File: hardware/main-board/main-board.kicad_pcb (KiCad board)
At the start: 4 copper layers, 105 x 38 mm, 78 parts, among them J1 USB_B_Micro, J2 DNI, J3 Display Connector, J4 Conn_01x02, SW1 SW_Push, SW2 SW_Push, SW3 SW_Push, SW4 SW_Push, SW5 SW_Detect, U1 TSL2591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

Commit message: Change MCU component value to 64KB flash variant
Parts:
- U2: value STM32L052K6U6 -> STM32L052K8U6

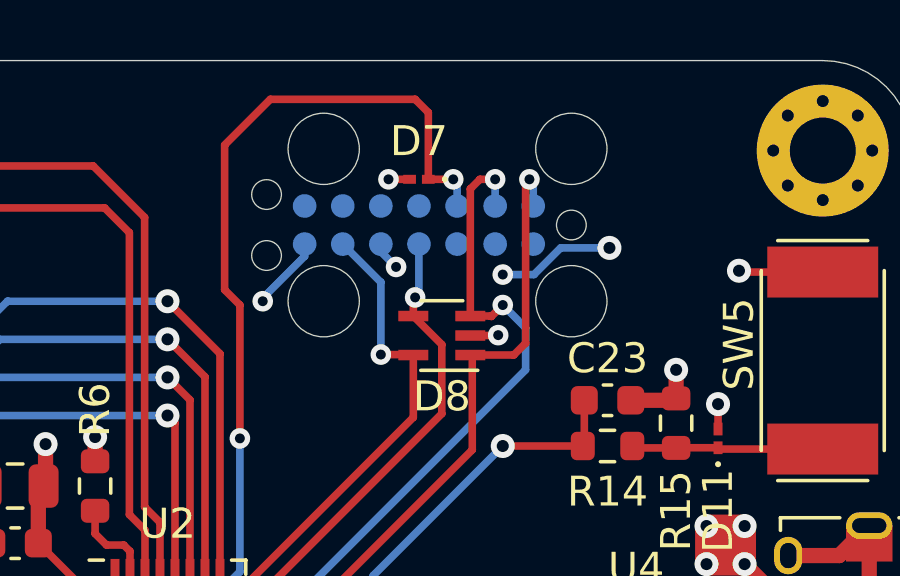
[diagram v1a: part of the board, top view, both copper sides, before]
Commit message: Connect power to debug connector
This allows the ST-Link to detect the target voltage, but otherwise
isn't really necessary. Still probably a good idea to have, though.
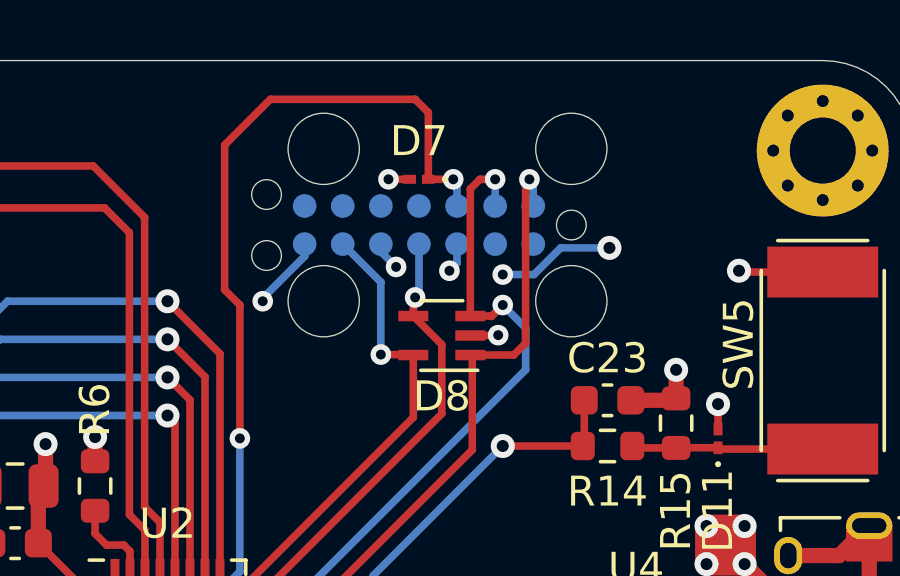
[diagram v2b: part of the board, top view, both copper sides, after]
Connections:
- J2 pad 3: Net-(J2-Pad3) -> +3V3
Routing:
- net +3V3: track 29.1 -> 30.1 mm, vias 10 -> 11

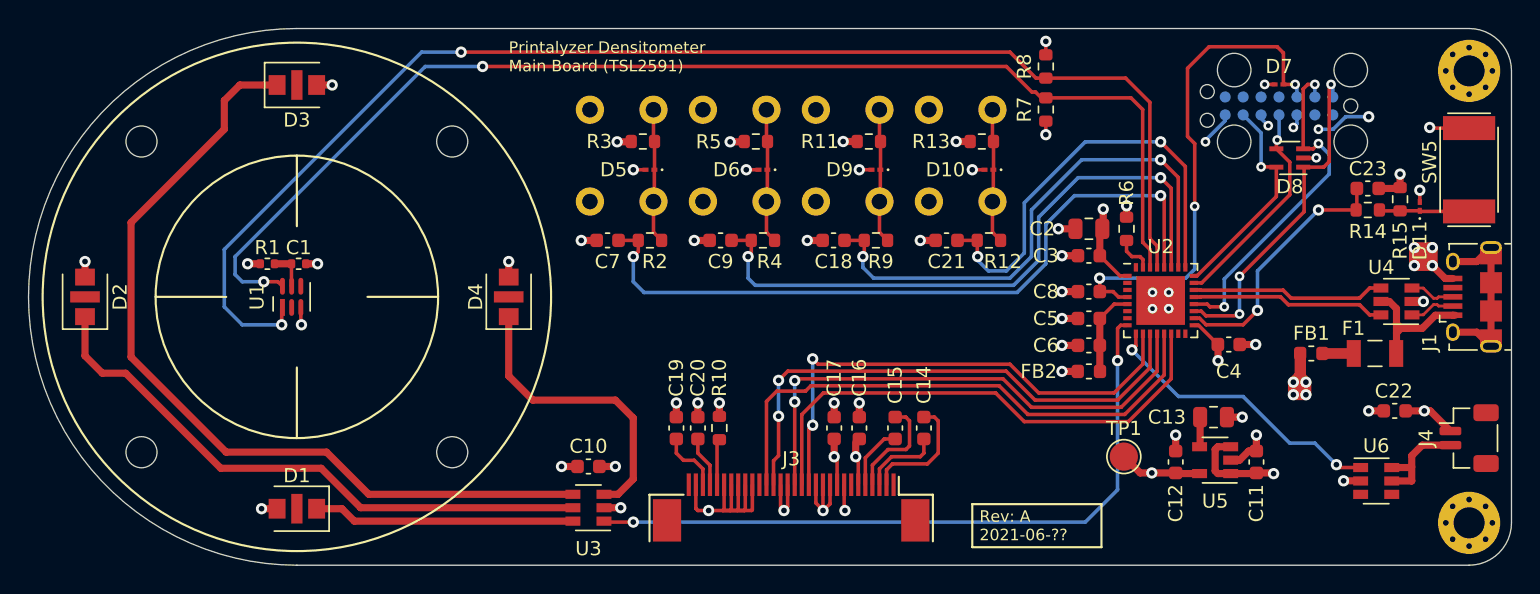
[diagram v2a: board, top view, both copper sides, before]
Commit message: Moved debug connector and minor trace cleanup
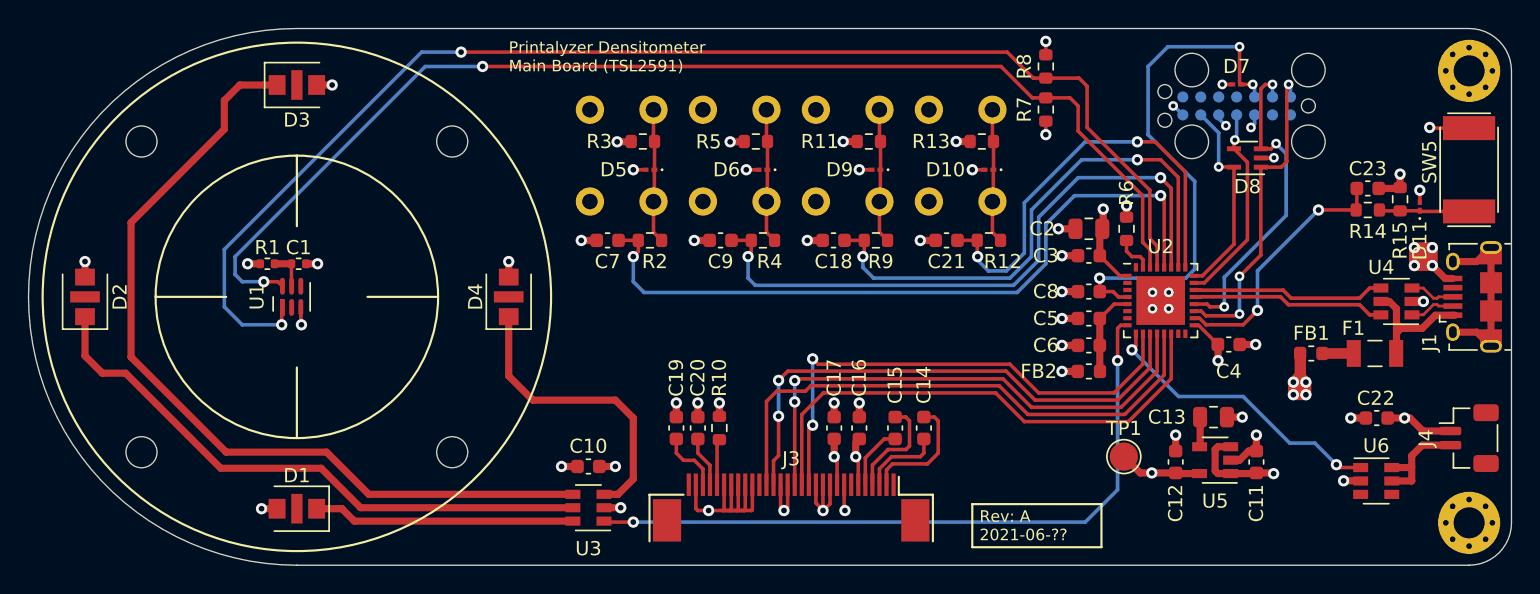
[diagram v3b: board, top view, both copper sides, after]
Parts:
- moved D7 3.00 mm to (126.5, 45.0)
- moved D8 3.00 mm to (127.3, 50.2)
- moved J2 3.00 mm to (126.5, 46.5)
- moved C22 1.37 mm to (136.5, 68.6)
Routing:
- net GND: track 74.5 -> 69.0 mm, vias 54 -> 52
- net /I2C1_SDA: track 87.5 -> 84.9 mm
- net /I2C1_SCL: track 94.6 -> 92.7 mm
- net /USART1_RX: track 24.4 -> 23.2 mm
- net /RESET: track 36.1 -> 37.3 mm
- net /USART1_TX: track 24.1 -> 22.9 mm
- net +5V: track 26.0 -> 27.2 mm
- net /SWDIO: track 15.5 -> 14.4 mm
- net /SWCLK: track 15.5 -> 14.8 mm

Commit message: Updated properties, silkscreen, and page markings for Rev A
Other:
- board text added: "Rev: A 2021-06-15"
- board text removed: "Rev: A 2021-06-??"
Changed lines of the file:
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@@
   (title_block
     (title "Printalyzer Densitometer - Main Board")
-    (date 2021-06-??)
+    (date 2021-06-15)
     (rev A)
     (company LogicProbe.org)
@@
     (pcbplotparams
       (layerselection 0x010fc_ffffffff)
-      (usegerberextensions false)
-      (usegerberattributes true)
-      (usegerberadvancedattributes true)
-      (creategerberjobfile true)
+      (usegerberextensions true)
+      (usegerberattributes false)
+      (usegerberadvancedattributes false)
+      (creategerberjobfile false)
       (excludeedgelayer true)
-      (linewidth 0.100000)
+      (linewidth 0.150000)
       (plotframeref false)
       (viasonmask false)
@@
       (plotvalue false)
       (plotinvisibletext false)
-      (padsonsilk true)
-      (subtractmaskfromsilk false)
+      (padsonsilk false)
+      (subtractmaskfromsilk true)
       (outputformat 1)
       (mirror false)
@@
       (effects (font (size 1 1) (thickness 0.15)))
     )
-    (pad MP smd roundrect (at 1.8 -1.2 270) (size 1.2 1.8) (layers F.Cu F.Paste F.Mask) (roundrect_rratio 0.208333))
-    (pad MP smd roundrect (at -1.8 -1.2 270) (size 1.2 1.8) (layers F.Cu F.Paste F.Mask) (roundrect_rratio 0.208333))
+    (pad MP smd roundrect (at 1.8 -1.2 270) (size 1.2 1.8) (layers F.Cu F.Paste F.Mask) (roundrect_rratio 0.2083325))
+    (pad MP smd roundrect (at -1.8 -1.2 270) (size 1.2 1.8) (layers F.Cu F.Paste F.Mask) (roundrect_rratio 0.2083325))
     (pad 2 smd roundrect (at 0.5 1.325 270) (size 0.6 1.55) (layers F.Cu F.Paste F.Mask) (roundrect_rratio 0.25)
       (net 68 "Net-(J4-Pad2)"))
@@
     (tags resistor)
     (attr smd)
-    (fp_text reference R6 (at 2.54 0 90) (layer F.SilkS)
+    (fp_text reference R6 (at 2.8575 0 90) (layer F.SilkS)
       (effects (font (size 1 1) (thickness 0.15)))
     )
@@
     (arrow2b (pts (xy 146 33.500001) (xy 144.873496 34.086422)))
   )
-  (gr_text "Rev: A\n2021-06-??" (at 114.284 67.585 180) (layer B.SilkS)
+  (gr_text "Rev: A\n2021-06-15" (at 114.284 67.585 180) (layer B.SilkS)
     (effects (font (size 0.8128 0.8128) (thickness 0.1524)) (justify left mirror))
   )
@@
   (gr_line (start 107.823 77.724) (end 116.967 77.724) (layer F.SilkS) (width 0.1524))
   (gr_line (start 107.823 74.676) (end 107.823 77.724) (layer F.SilkS) (width 0.1524))
-  (gr_text "Rev: A\n2021-06-??" (at 108.331 76.2) (layer F.SilkS)
+  (gr_text "Rev: A\n2021-06-15" (at 108.331 76.2) (layer F.SilkS)
     (effects (font (size 0.8128 0.8128) (thickness 0.1524)) (justify left))
   )

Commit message: Removed date and revision markings in prep for updates
This is to prevent old values from being left in the next revision. New
values will be added when Rev B is finished.
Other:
- board text added: "Rev: ? 2021-??-??"
- board text removed: "Rev: A 2021-06-15"

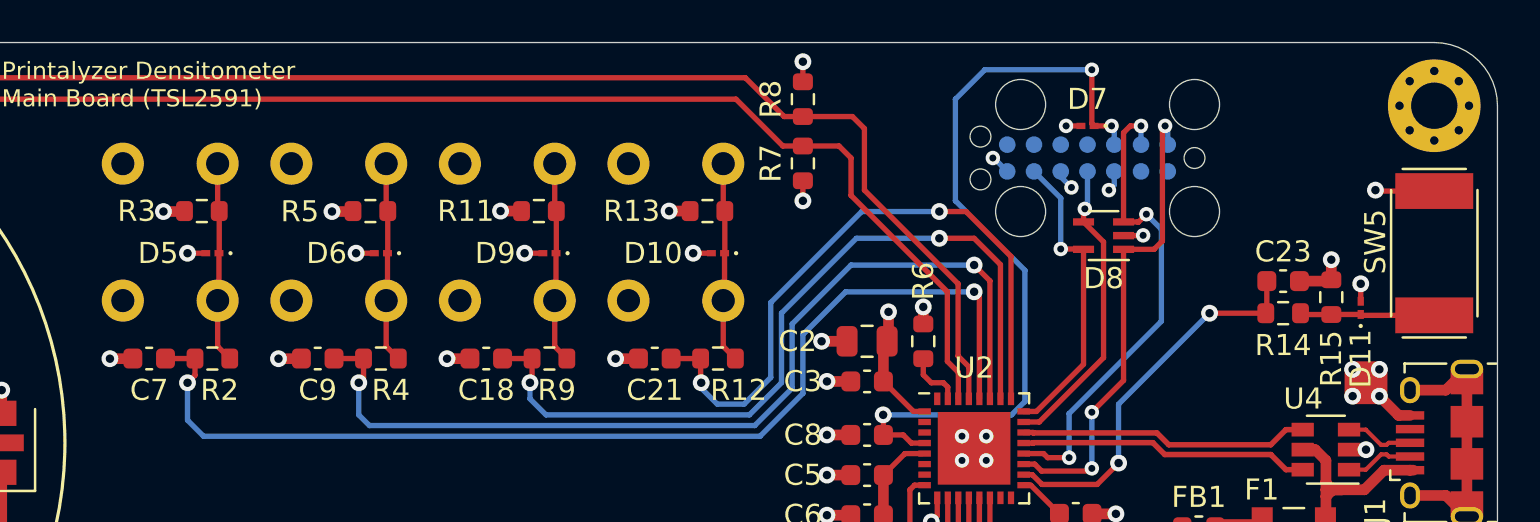
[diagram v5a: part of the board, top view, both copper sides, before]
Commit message: Switch single-line TVS diode components
Switch the existing single-line TVS diodes to a slightly larger
component.

Refs #10
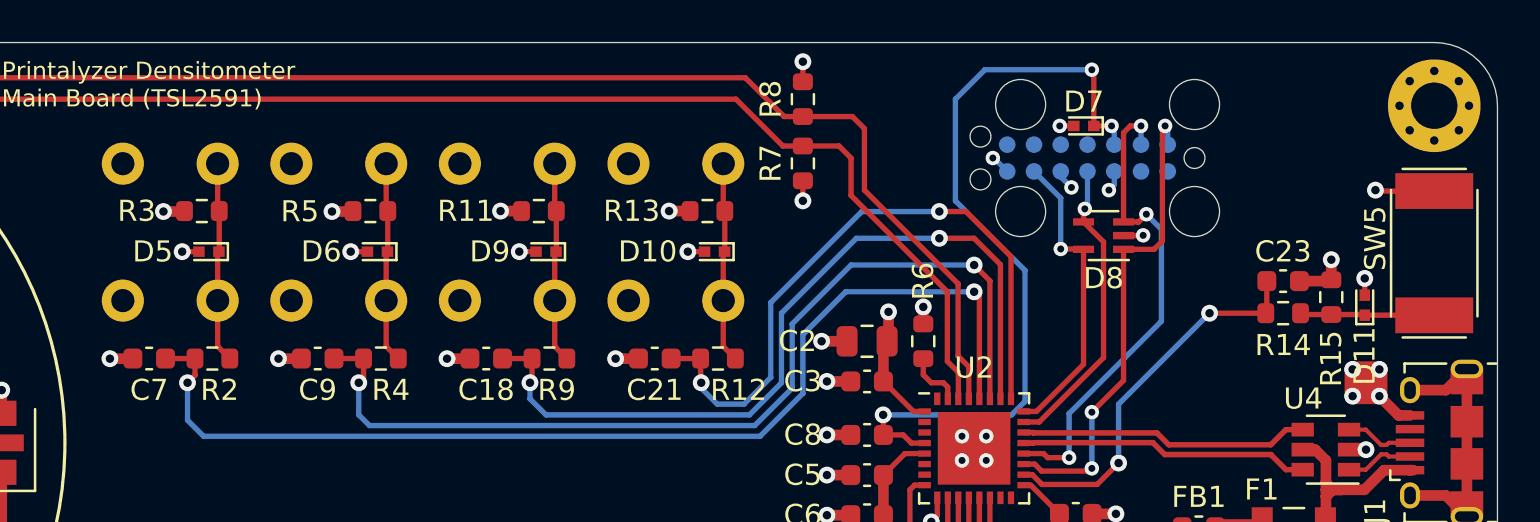
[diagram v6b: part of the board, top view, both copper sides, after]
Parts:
- D10, D11, D5, D6, D7, D9: value ESDALC6V1-1U2 -> ESDALC6V1-1M2; footprint lib_fp:ST0201 -> lib_fp:D_SOD-882
- moved D11 0.23 mm to (139.7, 53.5)
- moved D5 0.18 mm to (84.8, 50.9)
- moved D6 0.18 mm to (92.8, 50.9)
- moved D9 0.18 mm to (100.8, 50.9)
- moved D10 0.18 mm to (108.8, 50.9)
- moved D7 0.18 mm to (126.4, 45.0)

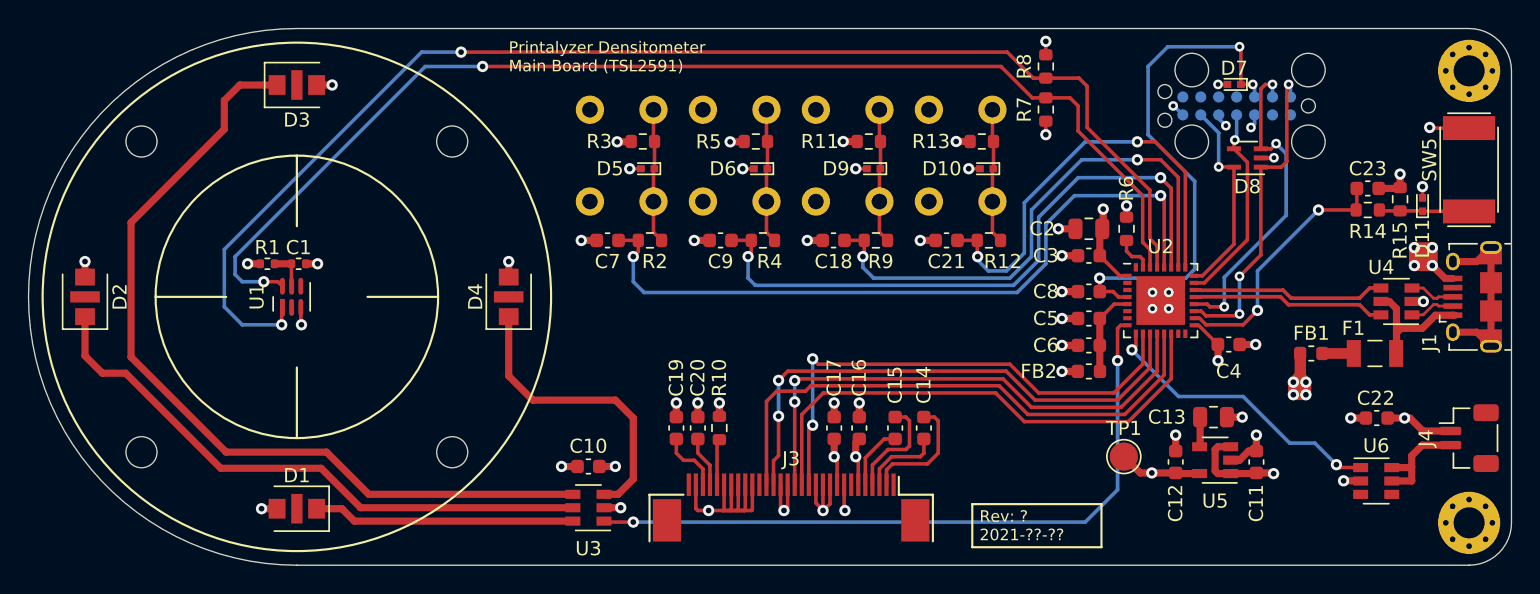
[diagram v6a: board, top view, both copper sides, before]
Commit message: Changed MCU on main board and routed pin changes
Swapped the MCU from the L052K to the K072K, pulling in all pin
assignment changes from the CubeMX data.

Added extra bypass capacitor and sensor interrupt (/w pull-up) to
schematic.

Updated PCB routing to reflect changes, which included rearranging the
layout of many bypass capacitors and making a variety of adjustments to
routing in the MCU area.

Left a placeholder for a BOOT0 selector button that will be added in the
future.

Note: Decided to stick with KiCad's stock QFN-32 footprint instead of
using the custom one (based on the ST datasheet) used in the previous
revision. This is because the pads on the KiCad footprint extend further
out from the part, which should resolve some issues with edge solder
contact that happened during prototype assembly.

Refs #8
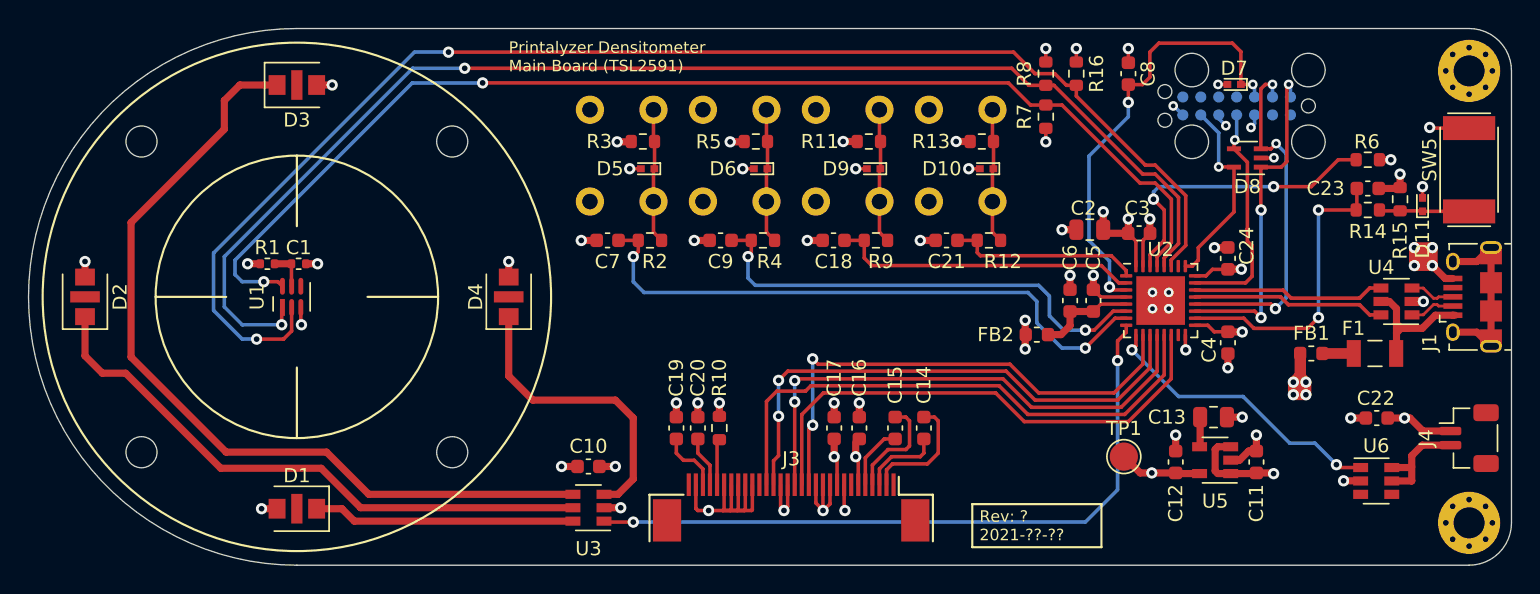
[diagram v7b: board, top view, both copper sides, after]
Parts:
- added C24: 0.1uF, Capacitor_SMD:C_0603_1608Metric, F.Cu at (125.9, 57.3)
- added R16: 10K, Resistor_SMD:R_0603_1608Metric, F.Cu at (115.2, 44.2)
- FB2: value 600R @ 100MHz -> 600R@100MHz
- U2: value STM32L052K8U6 -> STM32L072KBU6; footprint lib_fp:ST_UFQFPN32 -> Package_DFN_QFN:QFN-32-1EP_5x5mm_P0.5mm_EP3.45x3.45mm
- moved R6 17.8 mm to (135.8, 50.3), turned to 0 degrees
- moved C8 15.7 mm to (118.9, 44.2), turned to 90 degrees
- moved FB2 4.51 mm to (112.4, 62.7)
- moved C3 3.89 mm to (119.6, 55.5), turned to 0 degrees
- moved C6 3.44 mm to (114.7, 60.3), turned to 90 degrees
- moved C5 1.31 mm to (116.4, 60.3), turned to 90 degrees
- moved R7 0.51 mm to (113.0, 47.2)
- moved R8 0.51 mm to (113.0, 44.2)
- moved C4 0.14 mm to (125.9, 63.2), turned to 270 degrees
- moved C2 0.09 mm to (116.1, 55.2)
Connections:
- net Net-(C5-Pad1) renamed +3.3VA
- R6 pad 1: Net-(R6-Pad1) -> /BOOT0
- U1 pad 2: Net-(U1-Pad2) -> /TSL_INT
- U2 pad 1: +3V3 -> /BTN4
- U2 pad 16: Net-(U2-Pad16) -> GND
- U2 pad 2: Net-(U2-Pad2) -> /BTN3
- U2 pad 24: /SWCLK -> +3V3
- U2 pad 25: /BTN4 -> /SWCLK
- U2 pad 26: /BTN3 -> Net-(U2-Pad26)
- U2 pad 27: /BTN2 -> /TSL_INT
- U2 pad 28: /BTN1 -> /I2C1_SCL
- U2 pad 29: /I2C1_SCL -> /I2C1_SDA
- U2 pad 3: Net-(U2-Pad3) -> /RESET
- U2 pad 30: /I2C1_SDA -> /BOOT0
- U2 pad 31: Net-(R6-Pad1) -> GND
- U2 pad 32: Net-(U2-Pad32) -> +3V3
- U2 pad 4: /RESET -> GND
- U2 pad 6: Net-(U2-Pad6) -> /BTN2
- U2 pad 7: Net-(U2-Pad7) -> /BTN1
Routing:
- net /TSL_INT: track 0.00 -> 97.1 mm, vias 0 -> 2
- net /BOOT0: track 0.00 -> 21.3 mm, vias 0 -> 2
- net /BTN4: track 31.3 -> 13.7 mm, vias 2 -> 0
- net /BTN3: track 38.3 -> 21.9 mm, vias 2 -> 0
- net /BTN2: track 45.2 -> 33.9 mm
- net /BTN1: track 51.9 -> 43.2 mm
- net GND: track 68.7 -> 75.0 mm, vias 52 -> 54
- net +3V3: track 30.1 -> 36.2 mm, vias 11 -> 15
- net /RESET: track 37.4 -> 31.9 mm
- net /BTN5: track 18.2 -> 21.2 mm
- net Net-(R6-Pad1): track 2.72 -> 0.00 mm
- net /USART1_RX: track 23.2 -> 25.5 mm
- net /SWDIO: track 14.4 -> 16.4 mm
- net /USART1_TX: track 22.9 -> 24.1 mm
- net /I2C1_SCL: track 92.7 -> 91.7 mm
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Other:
- board text added: "Space reserved for BOOT0 select switch"
